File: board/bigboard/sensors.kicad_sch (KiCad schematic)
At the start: 2 parts

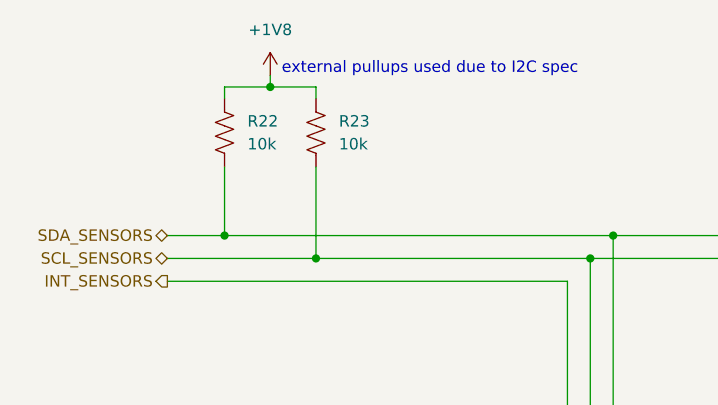
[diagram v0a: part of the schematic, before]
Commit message: Manufactured version of bigboard
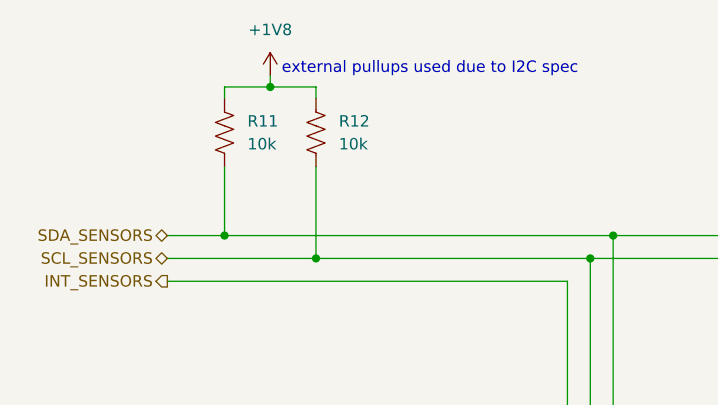
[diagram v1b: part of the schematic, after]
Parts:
- R11: renamed from R22; MPN (none) -> RC0201FR-0710KL
- R12: renamed from R23; MPN (none) -> RC0201FR-0710KL
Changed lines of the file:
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@@
   (symbol (lib_id "power:+1V8") (at 59.69 53.34 0) (unit 1)
     (in_bom yes) (on_board yes) (fields_autoplaced)
-    (property "Reference" "#PWR032" (id 0) (at 59.69 57.15 0)
+    (property "Reference" "#PWR028" (id 0) (at 59.69 57.15 0)
       (effects (font (size 1.27 1.27)) hide)
     )
@@
   (symbol (lib_id "Device:R_US") (at 54.61 59.69 0) (unit 1)
     (in_bom yes) (on_board yes) (fields_autoplaced)
-    (property "Reference" "R22" (id 0) (at 57.15 58.4199 0)
+    (property "Reference" "R11" (id 0) (at 57.15 58.4199 0)
       (effects (font (size 1.27 1.27)) (justify left))
     )
@@
       (effects (font (size 1.27 1.27)) hide)
     )
+    (property "MPN" "RC0201FR-0710KL" (id 5) (at 54.61 59.69 0)
+      (effects (font (size 1.27 1.27)) hide)
+    )
     (pin "1")
     (pin "2")
@@
   (symbol (lib_id "Device:R_US") (at 64.77 59.69 0) (unit 1)
     (in_bom yes) (on_board yes) (fields_autoplaced)
-    (property "Reference" "R23" (id 0) (at 67.31 58.4199 0)
+    (property "Reference" "R12" (id 0) (at 67.31 58.4199 0)
       (effects (font (size 1.27 1.27)) (justify left))
     )
@@
       (effects (font (size 1.27 1.27)) hide)
     )
+    (property "MPN" "RC0201FR-0710KL" (id 5) (at 64.77 59.69 0)
+      (effects (font (size 1.27 1.27)) hide)
+    )
